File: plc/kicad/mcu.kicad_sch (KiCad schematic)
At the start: 2 parts, among them U2 ESP32-S3-MINI-1U

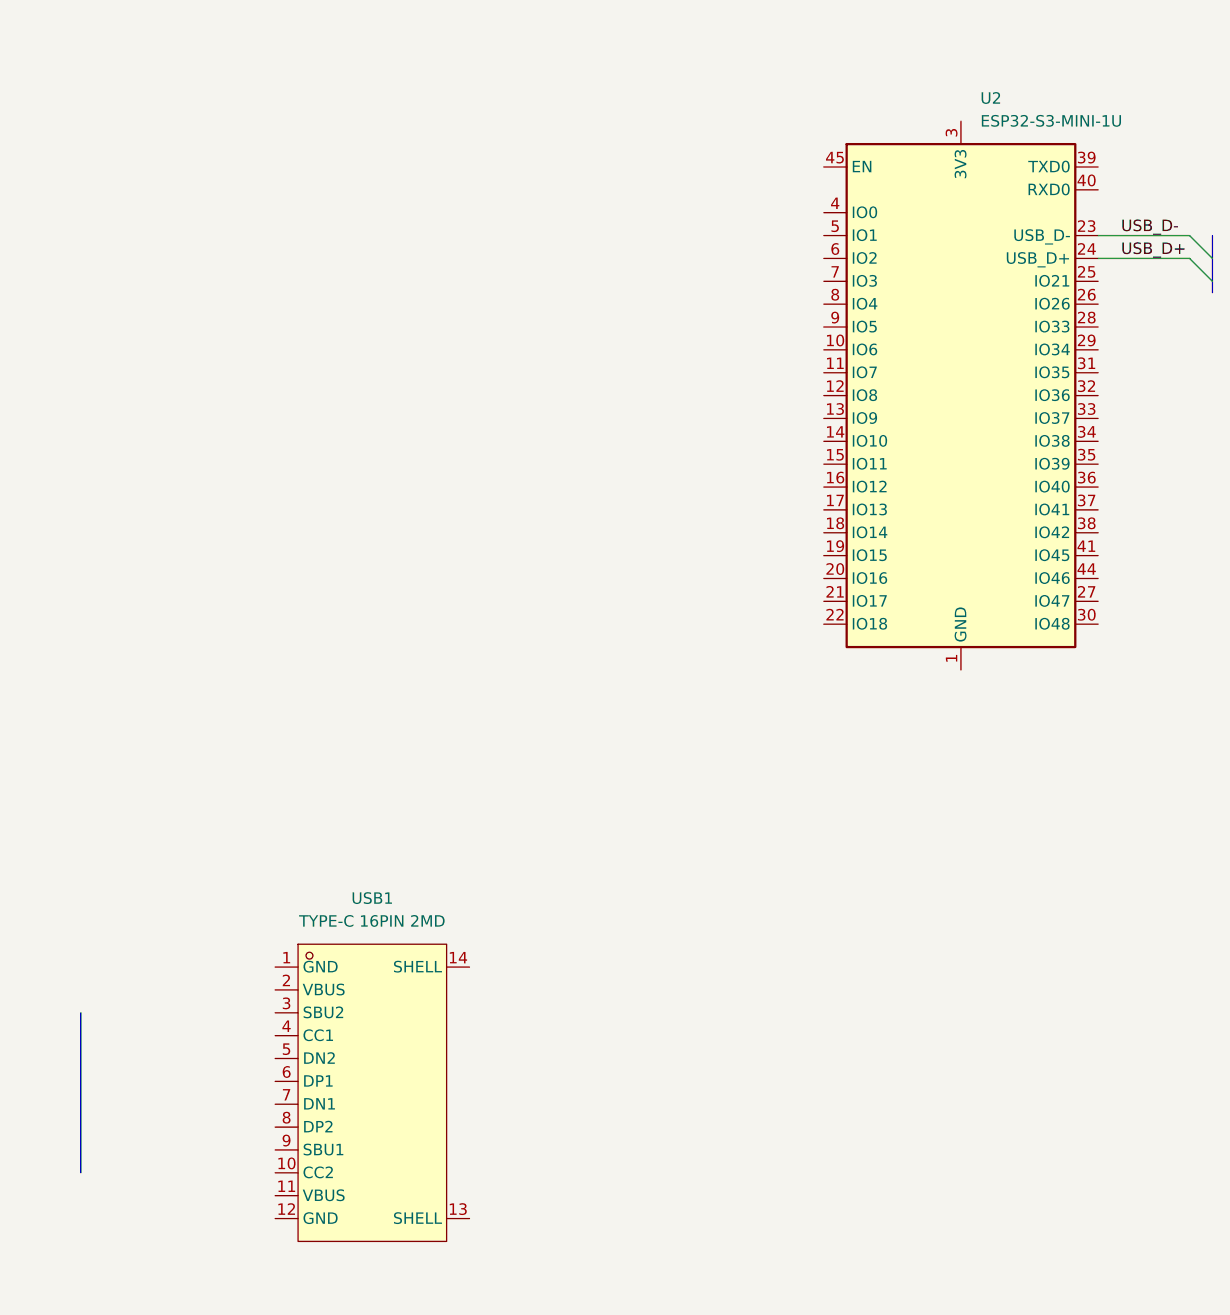
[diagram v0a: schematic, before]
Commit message: Added transistor outputs
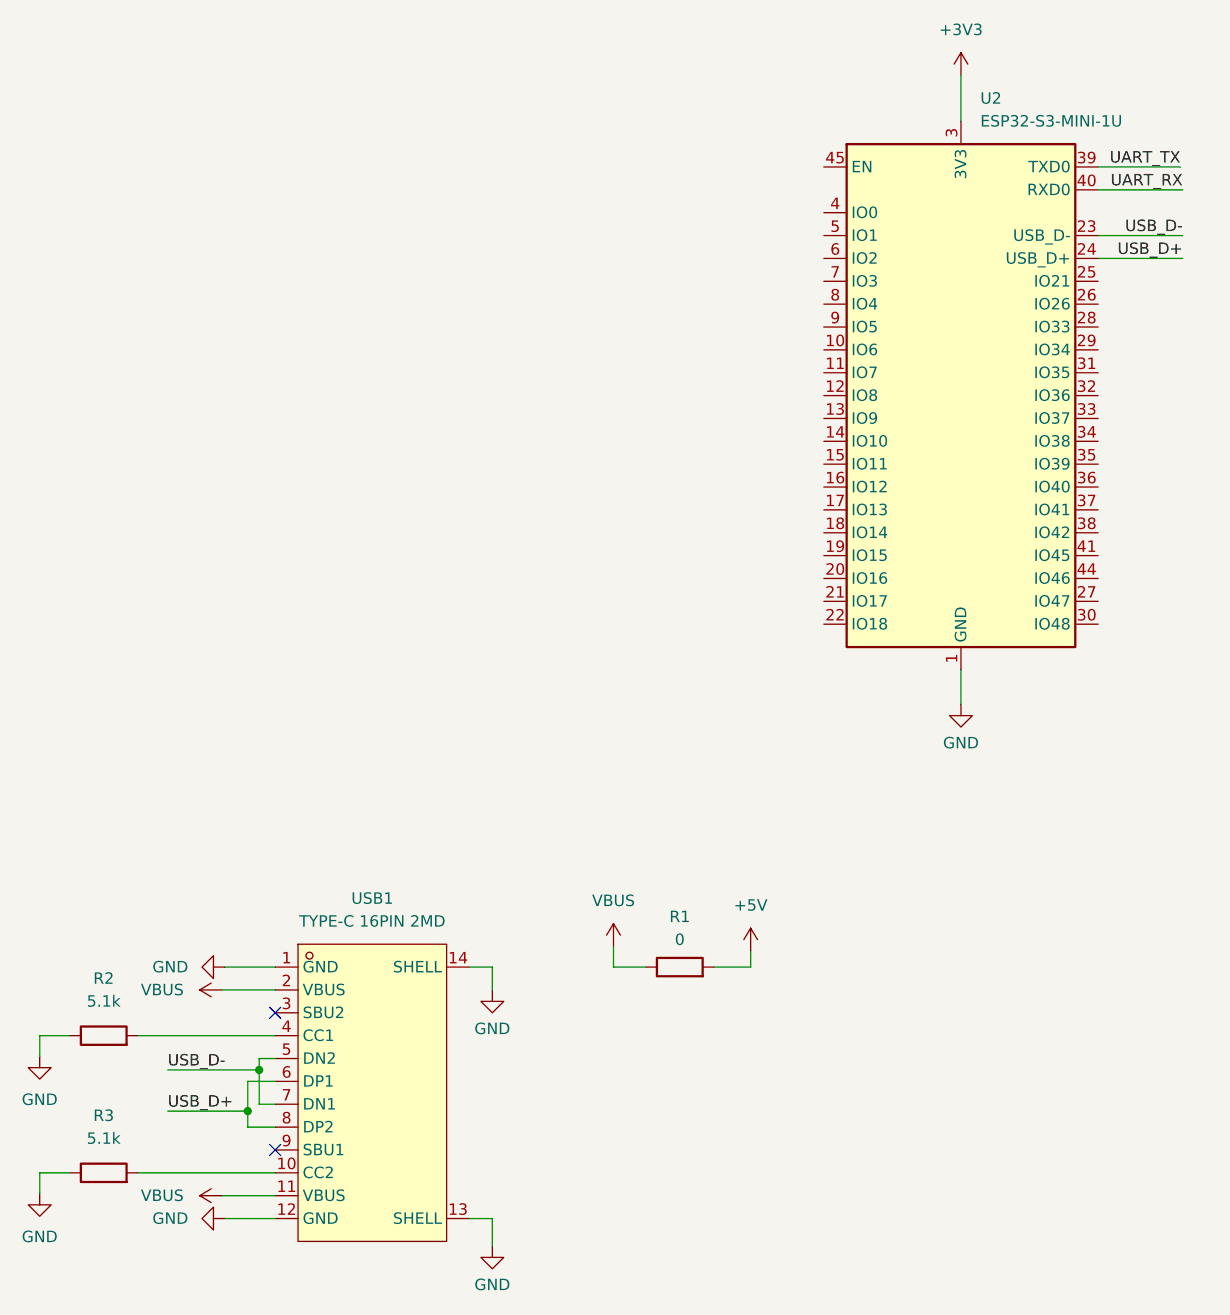
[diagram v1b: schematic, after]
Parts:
- added R1: 0, Jumper:SolderJumper-2_P1.3mm_Bridged2Bar_Pad1.0x1.5mm, symbol Device:R
- added R2, R3: 5.1k, Resistor_SMD:R_0805_2012Metric_Pad1.20x1.40mm_HandSolder, symbol Device:R
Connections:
- net USB_D+: now also USB1.6 (DP1), USB1.8 (DP2)
- net USB_D-: now also USB1.5 (DN2), USB1.7 (DN1)
- net GND: now reaches U2.1 (GND), U2.2 (GND), U2.42 (GND), U2.43 (GND), U2.46 (GND), U2.47 (GND), U2.48 (GND), U2.49 (GND), U2.50 (GND), U2.51 (GND), U2.52 (GND), U2.53 (GND), U2.54 (GND), U2.55 (GND), U2.56 (GND), U2.57 (GND), U2.58 (GND), U2.59 (GND), U2.60 (GND), U2.61 (GND), U2.62 (GND), U2.63 (GND), U2.64 (GND), U2.65 (GND)
- net GND: now also USB1.1 (GND), USB1.12 (GND), USB1.13 (SHELL), USB1.14 (SHELL), R2.1, R3.1
- net +3V3: now reaches U2.3 (3V3)
- net UART_TX: now reaches U2.39 (TXD0)
- net UART_RX: now reaches U2.40 (RXD0)
- net at USB1.10 (CC2): now also R3.2
- net VBUS: now reaches USB1.11 (VBUS)
- net VBUS: now also USB1.2 (VBUS), R1.1
- net at USB1.4 (CC1): now also R2.2
- new net +5V: R1.2
- no-connect marks 0 -> 2

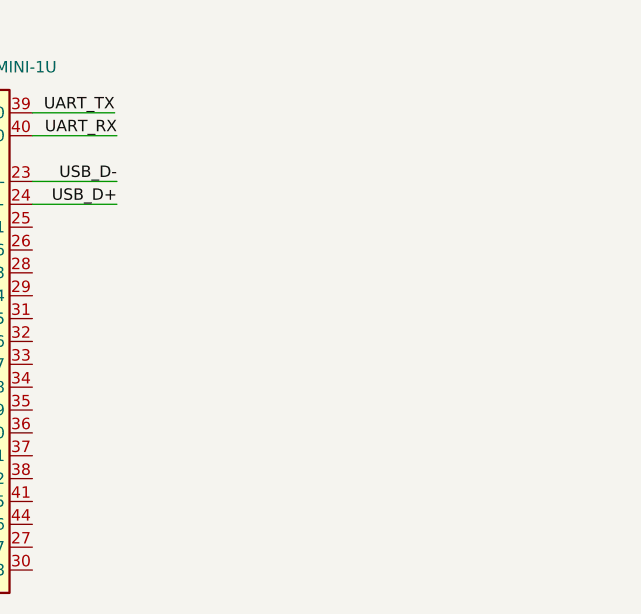
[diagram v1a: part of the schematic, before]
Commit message: Added gpio multiplexer and relay circuit
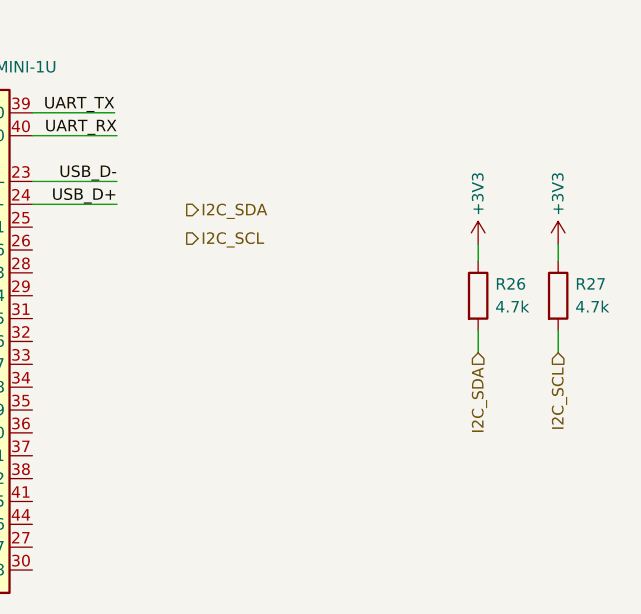
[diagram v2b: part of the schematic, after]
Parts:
- added R26, R27: 4.7k, Resistor_SMD:R_0805_2012Metric, symbol Device:R
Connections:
- net +3V3: now also R26.1, R27.1
- new net I2C_SCL: R27.2
- new net I2C_SDA: R26.2

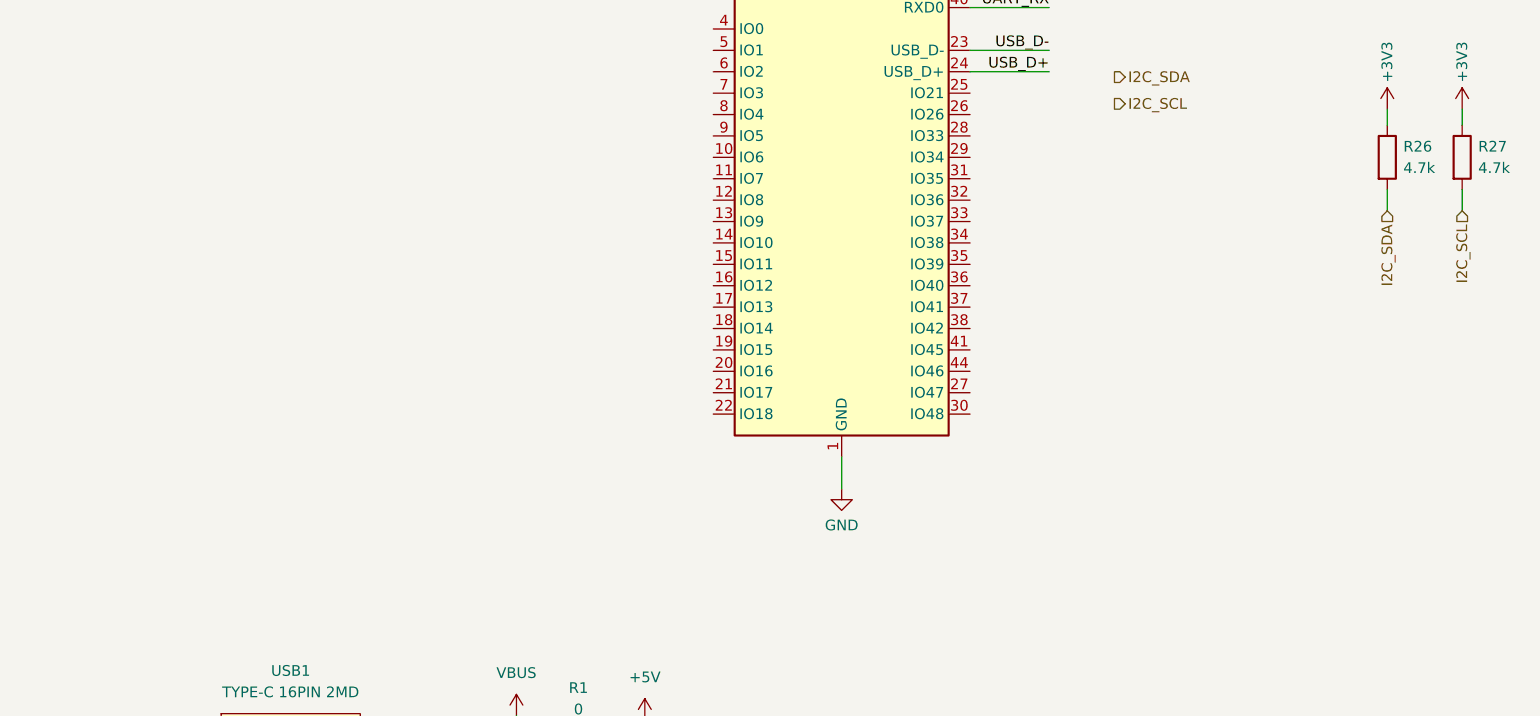
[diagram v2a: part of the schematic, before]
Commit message: Updated ethernet circuit
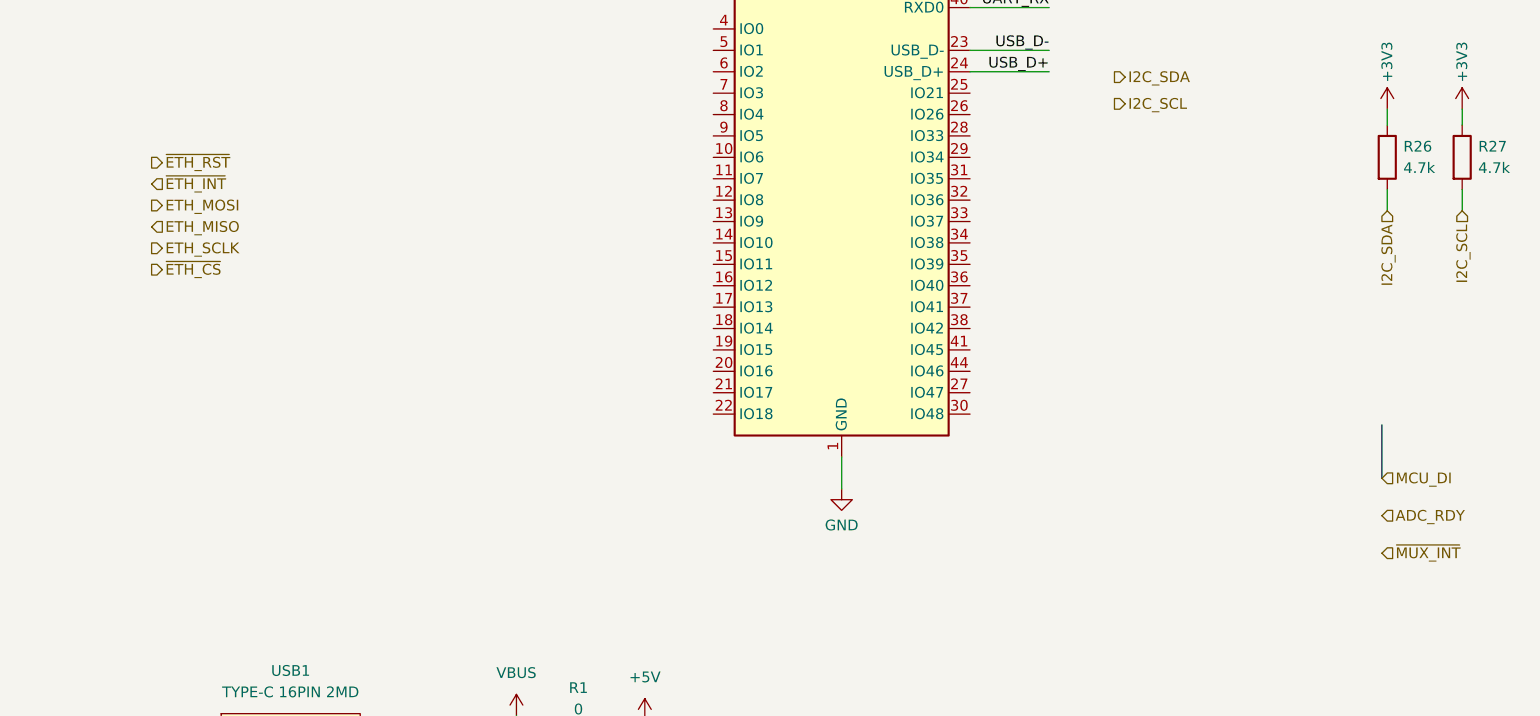
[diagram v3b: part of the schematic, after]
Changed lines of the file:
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@@
+		)
+	)
+	(bus
+		(pts
+			(xy 211.455 114.3) (xy 211.455 120.65)
+		)
+		(stroke
+			(width 0)
+			(type default)
 		)
 	)
@@
 		)
 	)
+	(hierarchical_label "ETH_MOSI"
+		(shape output)
+		(at 65.405 88.265 0)
+		(effects
+			(font
+				(size 1.27 1.27)
+			)
+			(justify left)
+		)
+	)
+	(hierarchical_label "~{ETH_CS}"
+		(shape output)
+		(at 65.405 95.885 0)
+		(effects
+			(font
+				(size 1.27 1.27)
+			)
+			(justify left)
+		)
+	)
+	(hierarchical_label "ADC_RDY"
+		(shape input)
+		(at 211.455 125.095 0)
+		(effects
+			(font
+				(size 1.27 1.27)
+			)
+			(justify left)
+		)
+	)
 	(hierarchical_label "I2C_SDA"
 		(shape input)
@@
 		)
 	)
+	(hierarchical_label "ETH_MISO"
+		(shape input)
+		(at 65.405 90.805 0)
+		(effects
+			(font
+				(size 1.27 1.27)
+			)
+			(justify left)
+		)
+	)
 	(hierarchical_label "I2C_SDA"
 		(shape output)
@@
 		)
 	)
+	(hierarchical_label "ETH_SCLK"
+		(shape output)
+		(at 65.405 93.345 0)
+		(effects
+			(font
+				(size 1.27 1.27)
+			)
+			(justify left)
+		)
+	)
+	(hierarchical_label "~{MUX_INT}"
+		(shape input)
+		(at 211.455 129.54 0)
+		(effects
+			(font
+				(size 1.27 1.27)
+			)
+			(justify left)
+		)
+	)
 	(hierarchical_label "I2C_SCL"
 		(shape input)
@@
 		)
 	)
+	(hierarchical_label "~{ETH_RST}"
+		(shape output)
+		(at 65.405 83.185 0)
+		(effects
+			(font
+				(size 1.27 1.27)
+			)
+			(justify left)
+		)
+	)
+	(hierarchical_label "~{ETH_INT}"
+		(shape input)
+		(at 65.405 85.725 0)
+		(effects
+			(font
+				(size 1.27 1.27)
+			)
+			(justify left)
+		)
+	)
+	(hierarchical_label "MCU_DI"
+		(shape input)
+		(at 211.455 120.65 0)
+		(effects
+			(font
+				(size 1.27 1.27)
+			)
+			(justify left)
+		)
+	)

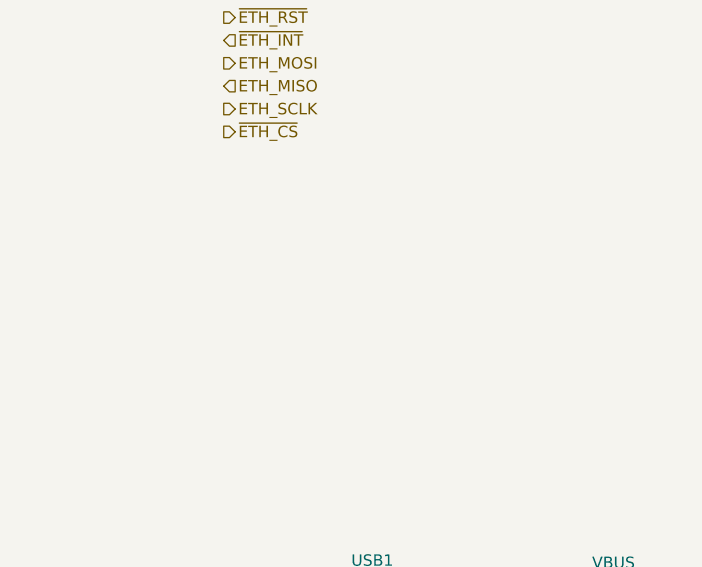
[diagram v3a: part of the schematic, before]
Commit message: Added RS 485 circuit
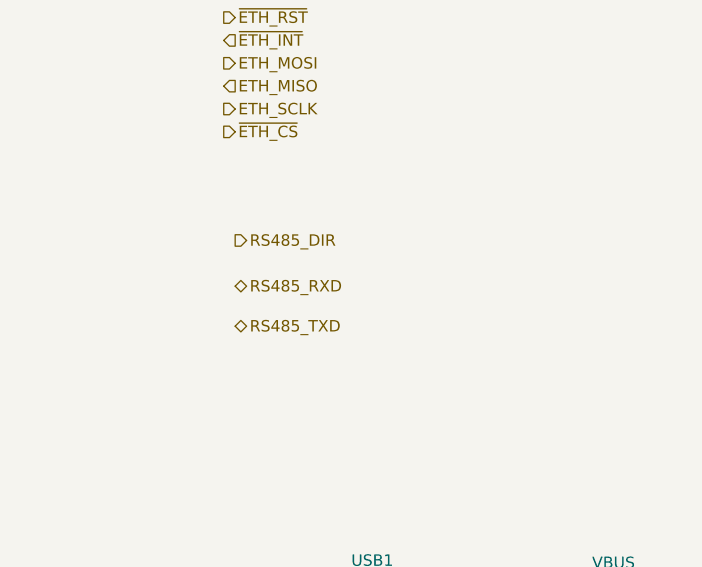
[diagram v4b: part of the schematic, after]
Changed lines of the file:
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@@
+		)
+	)
+	(hierarchical_label "RS485_TXD"
+		(shape bidirectional)
+		(at 66.675 117.475 0)
+		(effects
+			(font
+				(size 1.27 1.27)
+			)
+			(justify left)
 		)
 	)
@@
 		(effects
 			(font
+				(size 1.27 1.27)
+			)
+			(justify left)
+		)
+	)
+	(hierarchical_label "RS485_DIR"
+		(shape output)
+		(at 66.675 107.95 0)
+		(effects
+			(font
+				(size 1.27 1.27)
+			)
+			(justify left)
+		)
+	)
+	(hierarchical_label "RS485_RXD"
+		(shape bidirectional)
+		(at 66.675 113.03 0)
+		(effects
+			(font

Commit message: Added CAN circuit
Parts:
- removed R1: 0, Jumper:SolderJumper-2_P1.3mm_Bridged2Bar_Pad1.0x1.5mm, symbol Device:R

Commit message: Wired ESP32-S3 preliminarily
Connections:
- net ADC_RDY: now also U2.13 (IO9)
- net CAN_FAULT: now also U2.38 (IO42)
- net CAN_RX: now also U2.30 (IO48)
- net CAN_TX: now also U2.27 (IO47)
- net ETH_MISO: now also U2.17 (IO13)
- net ETH_MOSI: now also U2.15 (IO11)
- net ETH_SCLK: now also U2.16 (IO12)
- net I2C_SCL: now also U2.29 (IO34)
- net I2C_SDA: now also U2.28 (IO33)
- net RS485_DIR: now also U2.25 (IO21)
- net RS485_RXD: now also U2.21 (IO17)
- net RS485_TXD: now also U2.22 (IO18)
- net ~{ETH_CS}: now also U2.18 (IO14)
- net ~{ETH_INT}: now also U2.19 (IO15)
- net ~{ETH_RST}: now also U2.20 (IO16)
- net ~{MUX_INT}: now also U2.14 (IO10)
- net MCU_DI1: now reaches U2.31 (IO35)
- net MCU_DI2: now reaches U2.32 (IO36)
- net MCU_DI3: now reaches U2.33 (IO37)
- net MCU_DI4: now reaches U2.34 (IO38)
